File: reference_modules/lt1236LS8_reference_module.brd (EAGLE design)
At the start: 100 x 80 mm, 0 parts

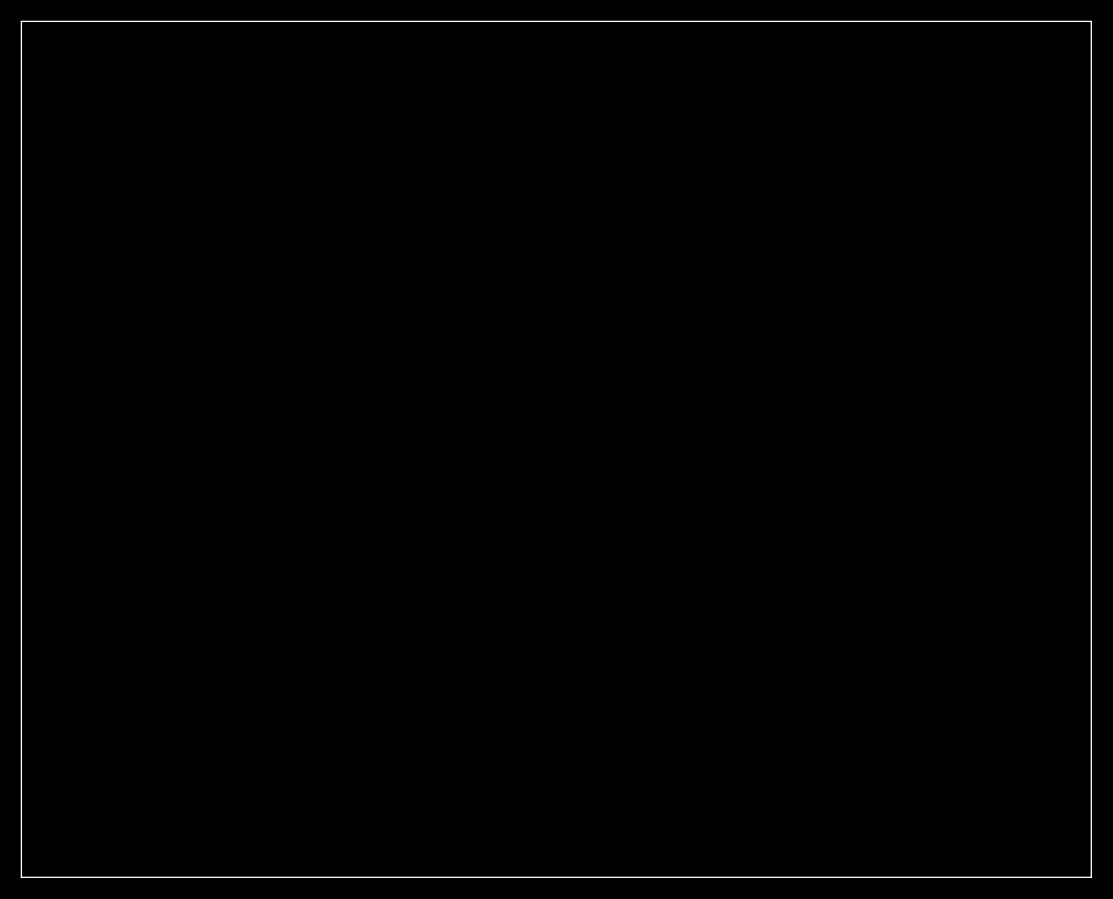
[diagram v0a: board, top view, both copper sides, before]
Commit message: * modified boards and processed for production
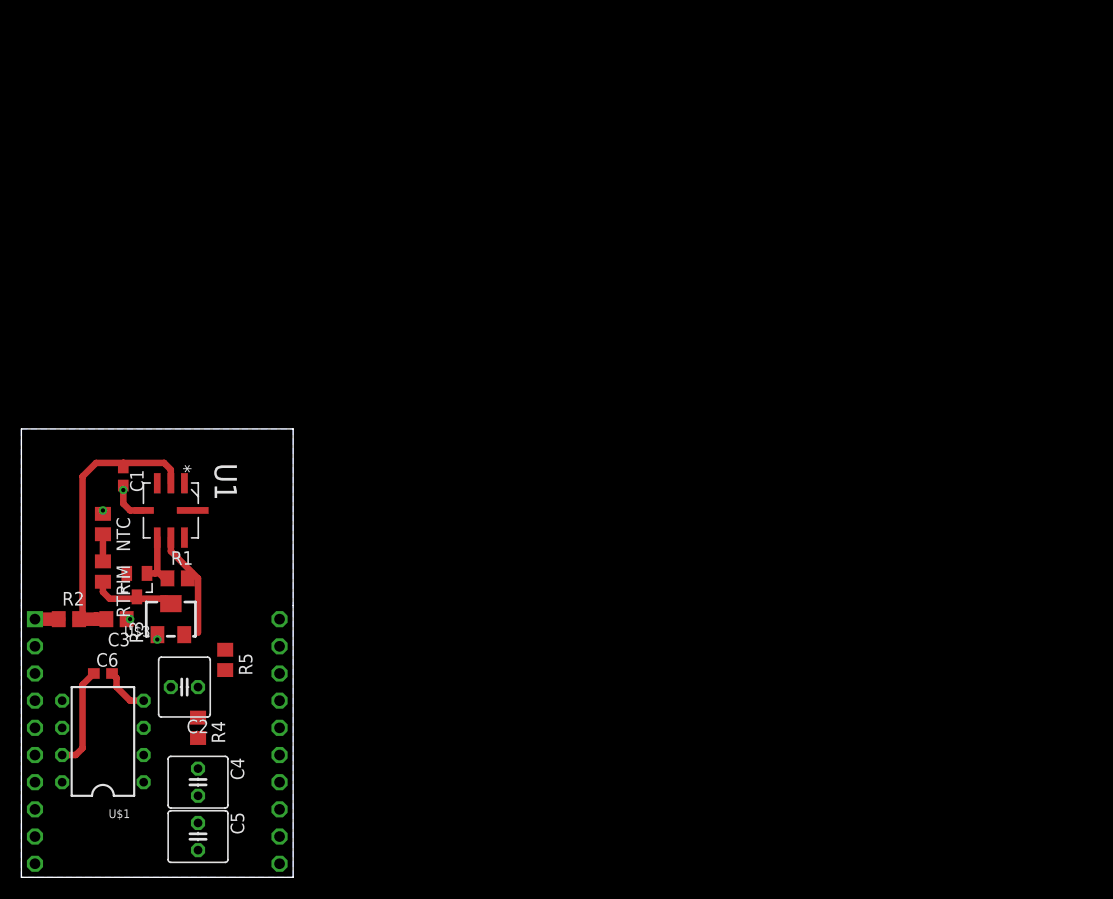
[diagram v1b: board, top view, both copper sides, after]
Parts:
- added C1, C6: 100n, SquantorRCL:C0603
- added C2, C4, C5: 1u, SquantorRCL:C025-060X050
- added C3: 10u, SquantorRCL:C0805
- added NTC, RTRIM: (no value), SquantorRCL:R0805
- added R1: 27k, SquantorRCL:R0805
- added R2: ferrite, SquantorRCL:R0805
- added R3: 50k, SquantorRCL:RTRIM3224W
- added R4, R5: 36k, SquantorRCL:R0805
- added U$1: LT1001, SquantorLinearTechnology:N8-PDIP8
- added U$2: METROLOGY_MODULE, SquantorPCBOutline:METROLOGY_MODULE
- added U$3: BAS17, SquantorNxp:SOT23_HAND
- added U1: LT1236BILS8-5PBFLS8_ELONG, SquantorLinearTechnology:LS8_ELONG
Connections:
- new net GND: C1.2, C3.1, C5.2, C6.2, NTC.1, R3.1, U$1.4, U$2.P$2, U$2.P$3, U$2.P$6, U1.4
- new net N$1: R2.1, U$2.P$1
- new net N$2: R3.2, RTRIM.2, U$3.3
- new net N$3: NTC.2, RTRIM.1
- new net N$5: C2.1, R4.1, R5.2
- new net N$6: C4.1, R4.2, U$1.3
- new net N$8: C4.2, C5.1
- new net VCC_VREF: C1.1, C3.2, C6.1, R2.2, U$1.7, U1.2
- new net VREF_IN: C2.2, U$1.2, U$2.P$4
- new net VREF_OUT: U$1.6, U$2.P$5
- new net VREF_OUT_UNFILT: R1.2, R3.3, R5.1, U1.6
- new net VREF_TRIM: R1.1, U$3.1, U1.5
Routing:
- net VCC_VREF: track 0.00 -> 36.6 mm
- net VREF_OUT_UNFILT: track 0.00 -> 9.94 mm
- net GND: track 0.00 -> 9.15 mm, vias 0 -> 4
- net N$2: track 0.00 -> 7.93 mm
- net VREF_TRIM: track 0.00 -> 5.42 mm
- net N$3: track 0.00 -> 2.55 mm
- net N$1: track 0.00 -> 2.23 mm
- added copper zone on layer 16, net GND
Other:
- board size 100 x 80 mm -> 25.4 x 25.4 mm
